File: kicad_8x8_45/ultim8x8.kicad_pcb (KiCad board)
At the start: 2 copper layers, 80 parts, among them P1 Input1, P2 Output1, P5 Input2, P6 Output2, U01 APA102, U02 APA102, U03 APA102, U04 APA102, U05 APA102, U06 APA102, U07 APA102, U08 APA102, U09 APA102, U10 APA102, U11 APA102, U12 APA102, U13 APA102, U14 APA102, U15 APA102, U16 APA102, U17 APA102, U18 APA102, U19 APA102, U20 APA102, U21 APA102, U22 APA102, U23 APA102, U24 APA102, U25 APA102, U26 APA102, U27 APA102, U28 APA102, U29 APA102, U30 APA102, U31 APA102, U32 APA102, U33 APA102, U34 APA102, U35 APA102, U36 APA102, U37 APA102, U38 APA102, U39 APA102, U40 APA102, U41 APA102, U42 APA102, U43 APA102, U44 APA102, U45 APA102, U46 APA102, U47 APA102, U48 APA102, U49 APA102, U50 APA102, U51 APA102, U52 APA102, U53 APA102, U54 APA102, U55 APA102, U56 APA102, U57 APA102, U58 APA102, U59 APA102, U60 APA102, U61 APA102, U62 APA102, U63 APA102, U64 APA102

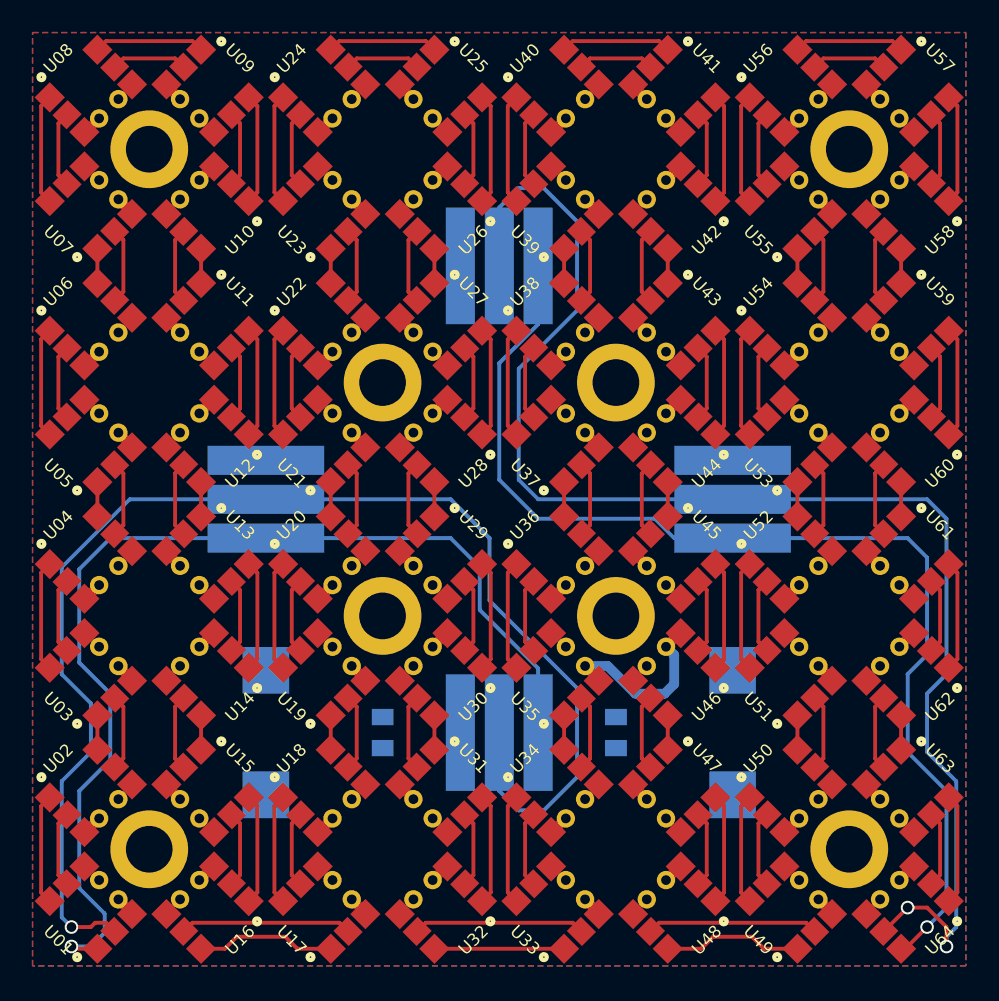
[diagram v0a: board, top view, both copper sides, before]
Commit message: angled LED version complete
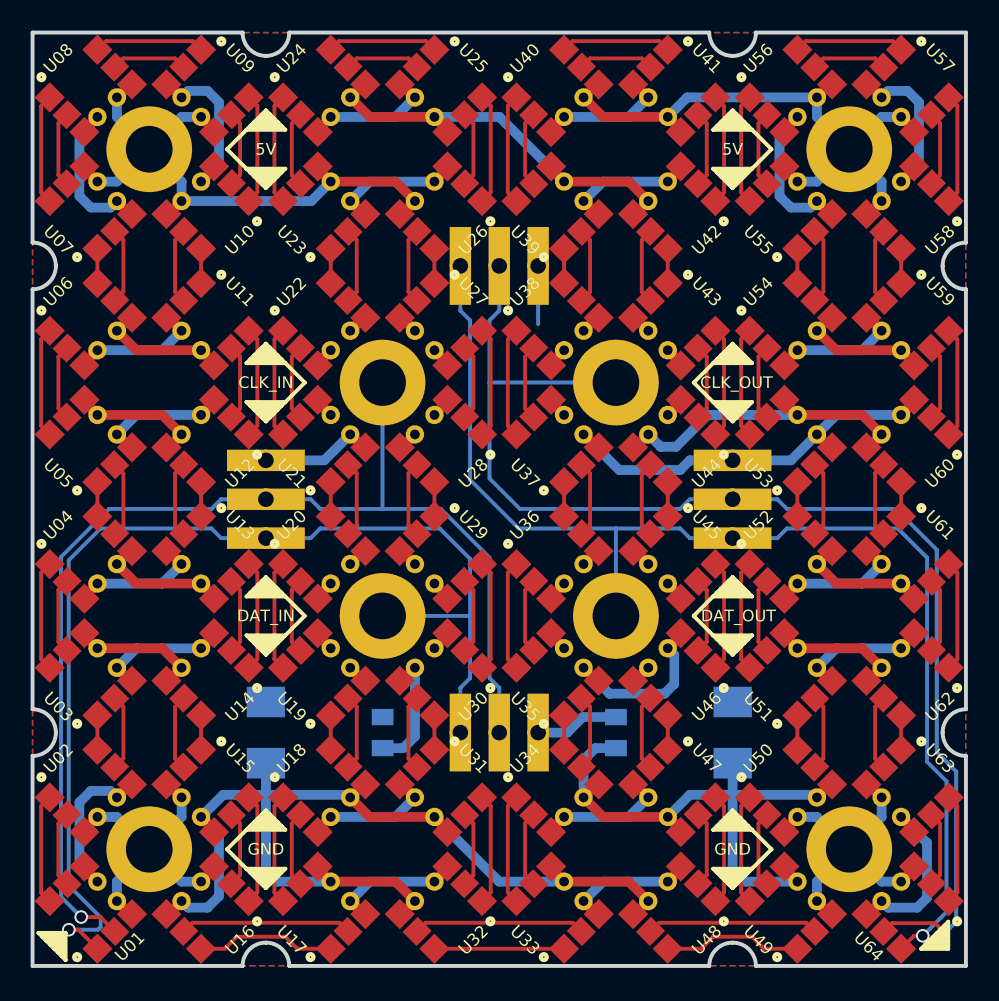
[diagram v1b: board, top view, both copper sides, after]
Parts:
- added L1: ULTiM8x8, ultim8x8_libs:logo_ultim8x8, B.Cu at (59.7, 59.7)
- added L2: OSHW, ultim8x8_libs:OSHW_6mm, B.Cu at (59.7, 33.3)
- added L3: Wyolum, ultim8x8_libs:logo_wyo_butterfly, B.Cu at (75.9, 44.5)
- added L4: Maniacal Labs, ultim8x8_libs:logo_MLlabs, B.Cu at (36.8, 72.4)
- C2, C4: footprint ultim8x8_libs:c_2917 -> ultim8x8_libs:C_1210_HandSoldering
- P1, P2, P5, P6: footprint ultim8x8_libs:header_3pos_smd_male -> ultim8x8_libs:header_3pos_th_male
- P10: renamed from S1; value CONN_1 -> DO_H; footprint ultim8x8_libs:Screw_SSide_2 -> ultim8x8_libs:Screw
- P11, P3: renamed from S1; value CONN_1 -> 5V; footprint ultim8x8_libs:Screw_SSide_2 -> ultim8x8_libs:Screw
- P12, P4: renamed from S1; value CONN_1 -> GND; footprint ultim8x8_libs:Screw_SSide_2 -> ultim8x8_libs:Screw
- P7: renamed from S1; value CONN_1 -> CI_A; footprint ultim8x8_libs:Screw_SSide_2 -> ultim8x8_libs:Screw
- P8: renamed from S1; value CONN_1 -> CO_H; footprint ultim8x8_libs:Screw_SSide_2 -> ultim8x8_libs:Screw
- P9: renamed from S1; value CONN_1 -> DI_A; footprint ultim8x8_libs:Screw_SSide_2 -> ultim8x8_libs:Screw
- turned C2 to 90 degrees
- turned C4 to 90 degrees
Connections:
- P10 pad 1: (no net) -> /Row_H/DO_H
- P11 pad 1: (no net) -> /Row_A/5V
- P12 pad 1: (no net) -> GND
- P2 pad 1: GND -> /Row_H/DO_H
- P2 pad 3: /Row_H/DO_H -> GND
- P3 pad 1: (no net) -> /Row_A/5V
- P4 pad 1: (no net) -> GND
- P5 pad 1: /Row_A/DI_A -> GND
- P5 pad 3: GND -> /Row_A/DI_A
- P7 pad 1: (no net) -> /Row_A/CI_A
- P8 pad 1: (no net) -> /Row_H/CO_H
- P9 pad 1: (no net) -> /Row_A/DI_A
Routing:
- net /Row_A/5V: track 0.00 -> 350.5 mm
- net GND: track 94.7 -> 292.9 mm
- net /Row_A/CI_A: track 87.6 -> 77.7 mm
- net /Row_H/CO_H: track 93.8 -> 85.0 mm, vias 2 -> 1
- net /Row_H/DO_H: track 73.6 -> 80.1 mm
- net /Row_A/DI_A: track 70.6 -> 75.1 mm
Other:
- board outline added: 61 x 61 mm
- board text added: "5V"
- board text added: "CLK_IN"
- board text added: "CLK_OUT"
- board text added: "DAT_IN"
- board text added: "DAT_OUT"
- board text added: "DO_H CO_H GND"
- board text added: "GND"
- board text added: "GND CI_A DI_A"
- board text added: "wyolum.com maniacallabs.com"
